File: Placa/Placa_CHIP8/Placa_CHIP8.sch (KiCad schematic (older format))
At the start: 10 parts, among them J1 Conn_01x08_Male-Teclado-Matri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, J2 Conn_01x06_Female-SD, J3 Conn_01x20_Female_LCD, J4 Conn_01x03_Male-UART, Q1 BC337, U1 STM32F103C8Tx, U2 Fuente

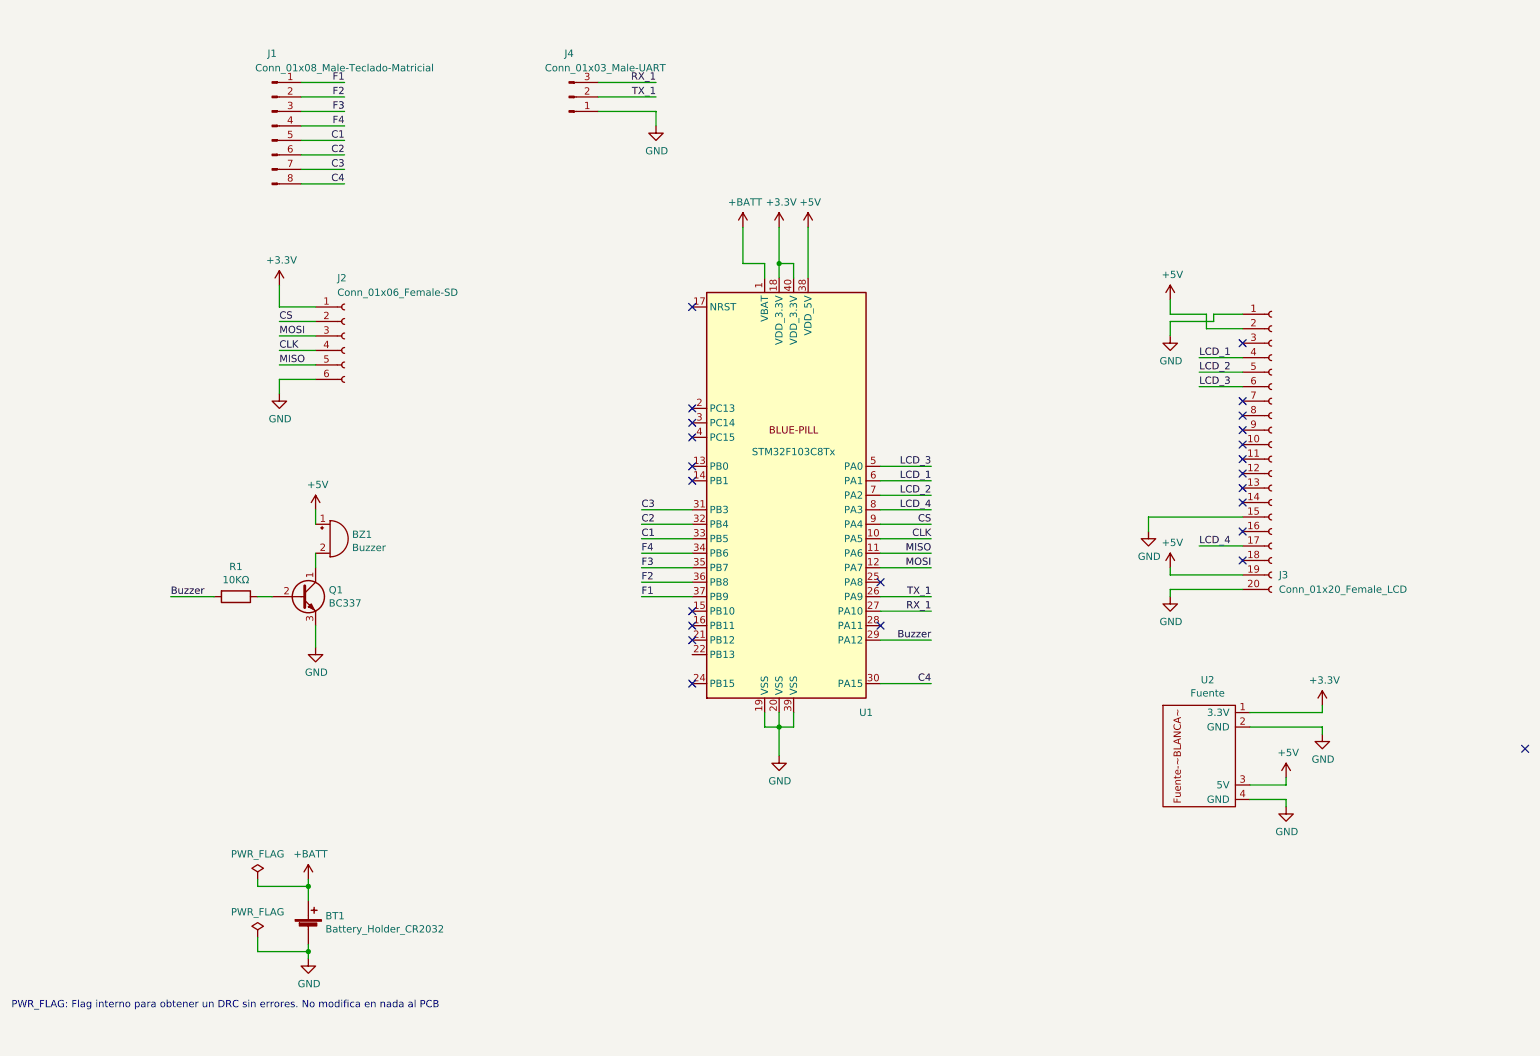
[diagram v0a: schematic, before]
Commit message: Modifico Placa con las conexiones nuevas
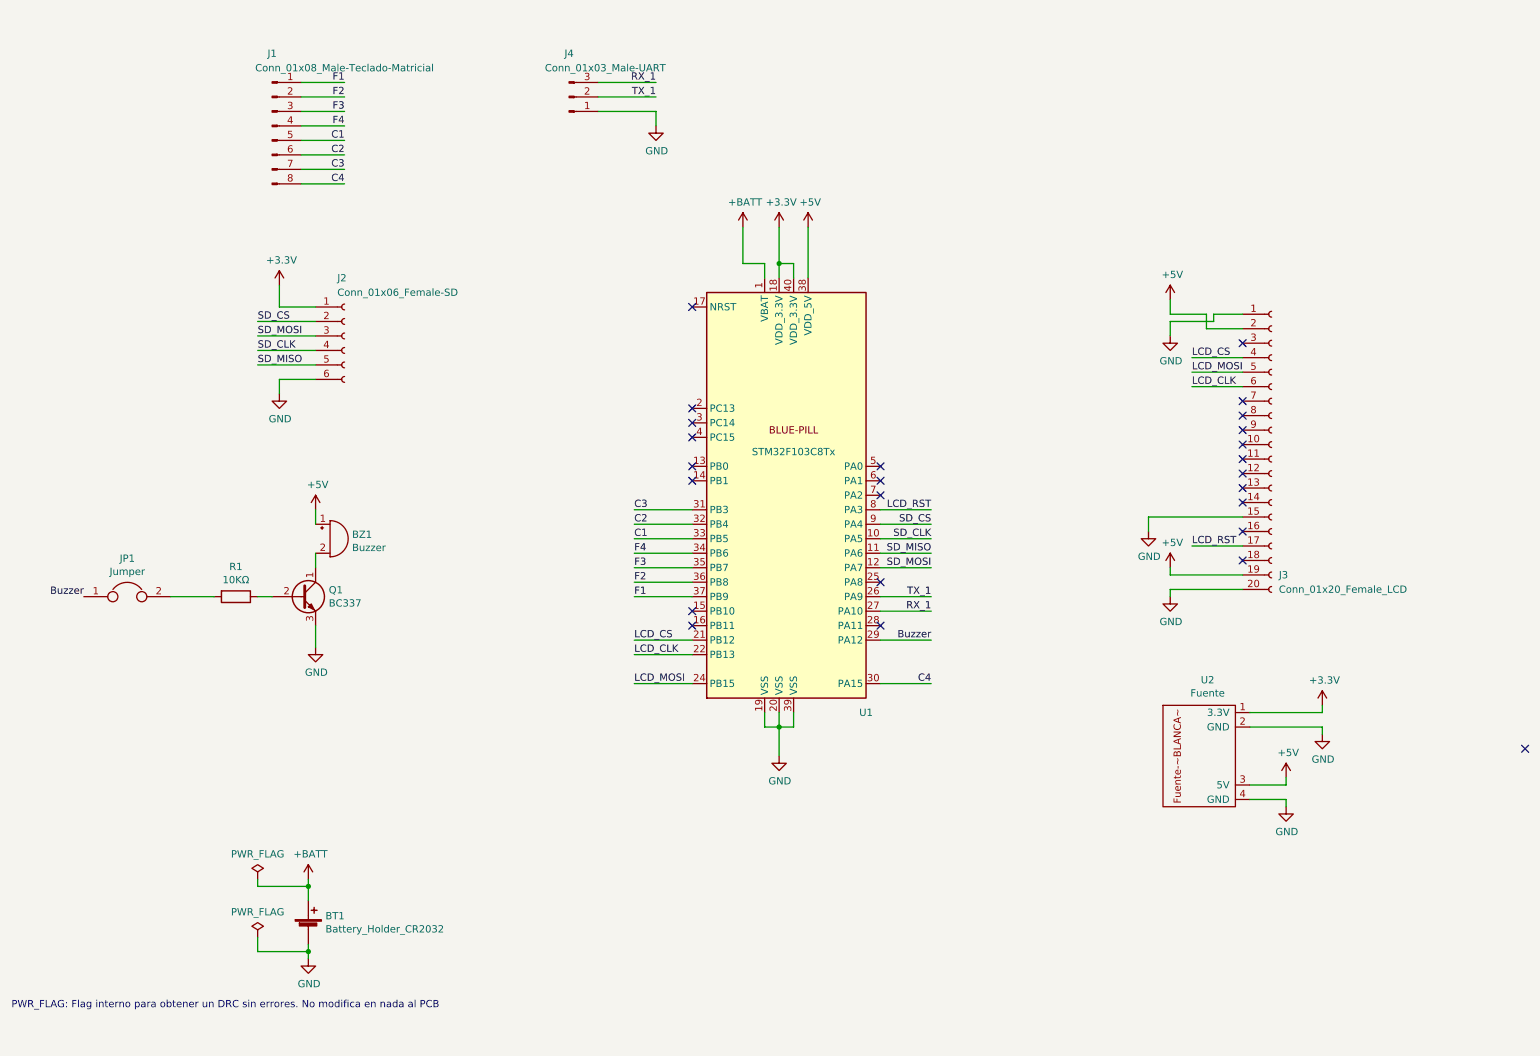
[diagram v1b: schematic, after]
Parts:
- added JP1: Jumper, symbol Device:Jumper
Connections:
- net Buzzer: now also JP1.1; no longer R1.2
- net LCD_CS: now reaches U1.21 (PB12)
- net LCD_CS: now also J3.4 (Pin_4)
- net LCD_CLK: now reaches U1.22 (PB13)
- net LCD_CLK: now also J3.6 (Pin_6)
- net LCD_MOSI: now reaches U1.24 (PB15)
- net LCD_MOSI: now also J3.5 (Pin_5)
- net CLK renamed SD_CLK
- net CS renamed SD_CS
- net LCD_1: no longer names the net of U1.6 (PA1)
- net LCD_1: no longer J3.4 (Pin_4)
- net LCD_2: no longer names the net of U1.7 (PA2)
- net LCD_2: no longer J3.5 (Pin_5)
- net LCD_3: no longer names the net of U1.5 (PA0)
- net LCD_3: no longer J3.6 (Pin_6)
- net LCD_4 renamed LCD_RST
- net MISO renamed SD_MISO
- net MOSI renamed SD_MOSI
- new net: JP1.2, R1.2
- no-connect marks 24 -> 25
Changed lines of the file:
@@
 Wire Wire Line
 	3100 1600 2800 1600
-Text Label 5150 3950 0    50   ~ 0
+Text Label 5100 3950 0    50   ~ 0
 C3
-Text Label 5150 4050 0    50   ~ 0
+Text Label 5100 4050 0    50   ~ 0
 C2
-Text Label 5150 4150 0    50   ~ 0
+Text Label 5100 4150 0    50   ~ 0
 C1
-Text Label 5150 4250 0    50   ~ 0
+Text Label 5100 4250 0    50   ~ 0
 F4
-Text Label 5150 4350 0    50   ~ 0
+Text Label 5100 4350 0    50   ~ 0
 F3
-Text Label 5150 4450 0    50   ~ 0
+Text Label 5100 4450 0    50   ~ 0
 F2
-Text Label 5150 4550 0    50   ~ 0
+Text Label 5100 4550 0    50   ~ 0
 F1
 Wire Wire Line
-	2900 2650 2650 2650
-Wire Wire Line
 	2900 2550 2650 2550
-Wire Wire Line
-	2900 2750 2650 2750
-Wire Wire Line
-	2900 2850 2650 2850
-Wire Wire Line
-	2900 2950 2650 2950
 Wire Wire Line
 	2900 3050 2650 3050
@@
 Wire Wire Line
 	2650 2400 2650 2550
-Text Label 2650 2950 0    50   ~ 0
-MISO
-Text Label 2650 2850 0    50   ~ 0
-CLK
-Text Label 2650 2750 0    50   ~ 0
-MOSI
-Text Label 2650 2650 0    50   ~ 0
-CS
+Text Label 2500 2950 0    50   ~ 0
+SD_MISO
+Text Label 2500 2850 0    50   ~ 0
+SD_CLK
+Text Label 2500 2750 0    50   ~ 0
+SD_MOSI
+Text Label 2500 2650 0    50   ~ 0
+SD_CS
 $Comp
 L Device:Buzzer BZ1
@@
 Wire Wire Line
 	2200 4550 1900 4550
-Text Label 1900 4550 0    50   ~ 0
+Text Label 1300 4550 2    50   ~ 0
 Buzzer
 $Comp
@@
 	2850 6950 2850 7000
 Wire Wire Line
-	9000 2900 9300 2900
-Wire Wire Line
-	9000 3000 9300 3000
-Wire Wire Line
-	9000 3100 9300 3100
-Wire Wire Line
 	9300 4400 8800 4400
 $Comp
@@
 Wire Wire Line
 	8800 4400 8800 4350
-Wire Wire Line
-	9300 4200 9000 4200
 $Comp
 L power:GND #PWR0110
@@
 NoConn ~ 9300 4100
 NoConn ~ 9300 4300
-Text Label 9000 2900 0    50   ~ 0
-LCD_1
-Text Label 9000 3000 0    50   ~ 0
-LCD_2
-Text Label 9000 3100 0    50   ~ 0
-LCD_3
-Text Label 9000 4200 0    50   ~ 0
-LCD_4
+Text Label 8950 2900 0    50   ~ 0
+LCD_CS
+Text Label 8950 4200 0    50   ~ 0
+LCD_RST
 Text Label 7150 4850 2    50   ~ 0
 Buzzer
-Text Label 7150 3850 2    50   ~ 0
-LCD_2
 Text Label 7150 3950 2    50   ~ 0
-LCD_4
-Text Label 7150 3750 2    50   ~ 0
-LCD_1
-Text Label 7150 3650 2    50   ~ 0
-LCD_3
+LCD_RST
 Text Label 7150 4050 2    50   ~ 0
-CS
+SD_CS
 Text Label 7150 4150 2    50   ~ 0
-CLK
-Text Label 7150 4250 2    50   ~ 0
-MISO
-Text Label 7150 4350 2    50   ~ 0
-MOSI
+SD_CLK
 $Comp
 L power:+5V #PWR0111
@@
 NoConn ~ 6800 4750
 NoConn ~ 5500 4650
-NoConn ~ 5500 4750
-NoConn ~ 5500 4850
-NoConn ~ 5500 5150
 NoConn ~ 5500 3750
 NoConn ~ 5500 3650
@@
 PWR_FLAG: Flag interno para obtener un DRC sin errores. No modifica en nada al PCB
 Wire Wire Line
-	6800 3650 7150 3650
-Wire Wire Line
-	6800 3750 7150 3750
-Wire Wire Line
-	6800 3850 7150 3850
-Wire Wire Line
 	6800 3950 7150 3950
 Wire Wire Line
@@
 Wire Wire Line
 	6800 5150 7150 5150
-Wire Wire Line
-	5150 4550 5500 4550
-Wire Wire Line
-	5150 4450 5500 4450
-Wire Wire Line
-	5150 4350 5500 4350
-Wire Wire Line
-	5150 4250 5500 4250
-Wire Wire Line
-	5150 4150 5500 4150
-Wire Wire Line
-	5150 4050 5500 4050
-Wire Wire Line
-	5150 3950 5500 3950
 Wire Wire Line
 	6800 4650 7150 4650
@@
 	1    0    0    -1
 $EndComp
+Wire Wire Line
+	2500 2650 2900 2650
+Wire Wire Line
+	2500 2750 2900 2750
+Wire Wire Line
+	2500 2850 2900 2850
+Wire Wire Line
+	2500 2950 2900 2950
+Text Label 7150 4250 2    50   ~ 0
+SD_MISO
+Text Label 7150 4350 2    50   ~ 0
+SD_MOSI
+NoConn ~ 5500 4750
+Text Label 5100 4850 0    50   ~ 0
+LCD_CS
+Text Label 5100 5150 0    50   ~ 0
+LCD_MOSI
+Wire Wire Line
+	5100 3950 5500 3950
+Wire Wire Line
+	5100 4050 5500 4050
+Wire Wire Line
+	5100 4150 5500 4150
+Wire Wire Line
+	5100 4250 5500 4250
+Wire Wire Line
+	5100 4350 5500 4350
+Wire Wire Line
+	5100 4450 5500 4450
+Wire Wire Line
+	5100 4550 5500 4550
+Wire Wire Line
+	5100 4850 5500 4850
+Wire Wire Line
+	5100 5150 5500 5150
+Wire Wire Line
+	5500 4950 5100 4950
+Text Label 5100 4950 0    50   ~ 0
+LCD_CLK
+NoConn ~ 6800 3650
+NoConn ~ 6800 3750
+NoConn ~ 6800 3850
+Wire Wire Line
+	8950 4200 9300 4200
+Wire Wire Line
+	8950 3100 9300 3100
+Wire Wire Line
+	9300 3000 8950 3000
+Wire Wire Line
+	8950 2900 9300 2900
+Text Label 8950 3000 0    50   ~ 0
+LCD_MOSI
+Text Label 8950 3100 0    50   ~ 0
+LCD_CLK
+$Comp
+L Device:Jumper JP1
+U 1 1 617816B8
+P 1600 4550
+F 0 "JP1" H 1600 4814 50  0000 C CNN
+F 1 "Jumper" H 1600 4723 50  0000 C CNN
+F 2 "" H 1600 4550 50  0001 C CNN
+F 3 "~" H 1600 4550 50  0001 C CNN
+	1    1600 4550
+	1    0    0    -1
+$EndComp

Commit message: modif
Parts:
- JP1: footprint (none) -> Connector_PinHeader_2.54mm:PinHeader_1x02_P2.54mm_Vertical
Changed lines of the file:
@@
 F 0 "JP1" H 1600 4814 50  0000 C CNN
 F 1 "Jumper" H 1600 4723 50  0000 C CNN
-F 2 "" H 1600 4550 50  0001 C CNN
+F 2 "Connector_PinHeader_2.54mm:PinHeader_1x02_P2.54mm_Vertical" H 1600 4550 50  0001 C CNN
 F 3 "~" H 1600 4550 50  0001 C CNN
 	1    1600 4550

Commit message: Agrego modelo Willy funcando ok y V1 gabinete
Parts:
- BT1: symbol Device:Battery_Cell -> Placa_CHIP8-rescue:Battery_Cell-Device
- BZ1: symbol Device:Buzzer -> Placa_CHIP8-rescue:Buzzer-Device
- J1: symbol Connector:Conn_01x08_Male -> Placa_CHIP8-rescue:Conn_01x08_Male-Connector
- J2: symbol Connector:Conn_01x06_Female -> Placa_CHIP8-rescue:Conn_01x06_Female-Connector
- J3: symbol Connector:Conn_01x20_Female -> Placa_CHIP8-rescue:Conn_01x20_Female-Connector
- J4: symbol Connector:Conn_01x03_Male -> Placa_CHIP8-rescue:Conn_01x03_Male-Connector
- JP1: symbol Device:Jumper -> Placa_CHIP8-rescue:Jumper-Device
- Q1: symbol Transistor_BJT:BC337 -> Placa_CHIP8-rescue:BC337-Transistor_BJT
- R1: symbol Device:R -> Placa_CHIP8-rescue:R-Device
- U1: symbol Placa:STM32F103C8Tx -> Placa_CHIP8-rescue:STM32F103C8Tx-Placa
- U2: symbol Placa:Fuente -> Placa_CHIP8-rescue:Fuente-Placa
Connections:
- wire segments 92 -> 98
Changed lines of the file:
@@
 $EndDescr
 $Comp
-L Connector:Conn_01x08_Male J1
+L Placa_CHIP8-rescue:Conn_01x08_Male-Connector J1
 U 1 1 61500CE4
 P 2600 1300
@@
 	2650 3050 2650 3150
 $Comp
-L power:GND #PWR0101
+L Placa_CHIP8-rescue:GND-power #PWR0101
 U 1 1 61511F8F
 P 2650 3150
@@
 $EndComp
 $Comp
-L power:+3.3V #PWR0102
+L Placa_CHIP8-rescue:+3.3V-power #PWR0102
 U 1 1 615124CF
 P 2650 2400
@@
 SD_CS
 $Comp
-L Device:Buzzer BZ1
+L Placa_CHIP8-rescue:Buzzer-Device BZ1
 U 1 1 61517873
 P 3000 4150
@@
 $EndComp
 $Comp
-L Transistor_BJT:BC337 Q1
+L Placa_CHIP8-rescue:BC337-Transistor_BJT Q1
 U 1 1 61518038
 P 2800 4550
@@
 $EndComp
 $Comp
-L power:GND #PWR0103
+L Placa_CHIP8-rescue:GND-power #PWR0103
 U 1 1 615193E1
 P 2900 4900
@@
 $EndComp
 $Comp
-L Device:R R1
+L Placa_CHIP8-rescue:R-Device R1
 U 1 1 61519A86
 P 2350 4550
@@
 $EndComp
 $Comp
-L power:+5V #PWR0104
+L Placa_CHIP8-rescue:+5V-power #PWR0104
 U 1 1 6151A6DF
 P 2900 3950
@@
 Wire Wire Line
 	2600 4550 2500 4550
-Wire Wire Line
-	2200 4550 1900 4550
 Text Label 1300 4550 2    50   ~ 0
 Buzzer
 $Comp
-L Device:Battery_Cell BT1
+L Placa_CHIP8-rescue:Battery_Cell-Device BT1
 U 1 1 615277F3
 P 2850 6850
@@
 $EndComp
 $Comp
-L power:GND #PWR0105
+L Placa_CHIP8-rescue:GND-power #PWR0105
 U 1 1 6152B7C4
 P 2850 7050
@@
 	9300 4400 8800 4400
 $Comp
-L power:+5V #PWR0108
+L Placa_CHIP8-rescue:+5V-power #PWR0108
 U 1 1 61553D8C
 P 8800 4350
@@
 $EndComp
 $Comp
-L power:GND #PWR0109
+L Placa_CHIP8-rescue:GND-power #PWR0109
 U 1 1 61554437
 P 8800 4550
@@
 	8800 4400 8800 4350
 $Comp
-L power:GND #PWR0110
+L Placa_CHIP8-rescue:GND-power #PWR0110
 U 1 1 6155A581
 P 8650 4100
@@
 SD_CLK
 $Comp
-L power:+5V #PWR0111
+L Placa_CHIP8-rescue:+5V-power #PWR0111
 U 1 1 61591E63
 P 9600 5800
@@
 $EndComp
 $Comp
-L power:GND #PWR0112
+L Placa_CHIP8-rescue:GND-power #PWR0112
 U 1 1 6159276C
 P 9600 6000
@@
 $EndComp
 $Comp
-L power:+3.3V #PWR0113
+L Placa_CHIP8-rescue:+3.3V-power #PWR0113
 U 1 1 6159301E
 P 9850 5300
@@
 $EndComp
 $Comp
-L power:GND #PWR0114
+L Placa_CHIP8-rescue:GND-power #PWR0114
 U 1 1 61593D3E
 P 9850 5500
@@
 	9600 5950 9600 6000
 $Comp
-L power:GND #PWR0115
+L Placa_CHIP8-rescue:GND-power #PWR0115
 U 1 1 615AC362
 P 6100 5650
@@
 	6100 5650 6100 5450
 $Comp
-L power:+3.3V #PWR0116
+L Placa_CHIP8-rescue:+3.3V-power #PWR0116
 U 1 1 615B6A0C
 P 6100 2000
@@
 NoConn ~ 11250 5600
 $Comp
-L power:+BATT #PWR0117
+L Placa_CHIP8-rescue:+BATT-power #PWR0117
 U 1 1 615E3802
 P 2850 6500
@@
 	2850 6500 2850 6550
 $Comp
-L power:+BATT #PWR0118
+L Placa_CHIP8-rescue:+BATT-power #PWR0118
 U 1 1 615E9338
 P 5850 2000
@@
 $EndComp
 $Comp
-L Placa:Fuente U2
+L Placa_CHIP8-rescue:Fuente-Placa U2
 U 1 1 615EFB9F
 P 9000 5650
@@
 $EndComp
 $Comp
-L Placa:STM32F103C8Tx U1
+L Placa_CHIP8-rescue:STM32F103C8Tx-Placa U1
 U 1 1 6160BC1E
 P 6200 3850
@@
 $EndComp
 $Comp
-L power:+5V #PWR0119
+L Placa_CHIP8-rescue:+5V-power #PWR0119
 U 1 1 61620457
 P 6300 2000
@@
 	2850 6550 2850 6650
 $Comp
-L power:PWR_FLAG #FLG0102
+L Placa_CHIP8-rescue:PWR_FLAG-power #FLG0102
 U 1 1 6162B3A1
 P 2500 6900
@@
 TX_1
 $Comp
-L Connector:Conn_01x03_Male J4
+L Placa_CHIP8-rescue:Conn_01x03_Male-Connector J4
 U 1 1 615256F9
 P 4650 1100
@@
 	5250 1200 5250 1300
 $Comp
-L power:GND #PWR0120
+L Placa_CHIP8-rescue:GND-power #PWR0120
 U 1 1 61533673
 P 5250 1300
@@
 	1    0    0    -1
 $EndComp
-Text Label 5250 1100 2    50   ~ 0
+Text Label 5550 1100 2    50   ~ 0
 TX_1
 Wire Wire Line
-	4850 1100 5250 1100
-Wire Wire Line
-	4850 1000 5250 1000
-Wire Wire Line
 	4850 1200 5250 1200
 $Comp
-L Connector:Conn_01x20_Female J3
+L Placa_CHIP8-rescue:Conn_01x20_Female-Connector J3
 U 1 1 6152DDD6
 P 9500 3500
@@
 $EndComp
 $Comp
-L power:GND #PWR0106
+L Placa_CHIP8-rescue:GND-power #PWR0106
 U 1 1 615368BB
 P 8800 2750
@@
 $EndComp
 $Comp
-L power:+5V #PWR0107
+L Placa_CHIP8-rescue:+5V-power #PWR0107
 U 1 1 6153D9CC
 P 8800 2500
@@
 	8800 2500 8800 2600
 $Comp
-L Connector:Conn_01x06_Female J2
+L Placa_CHIP8-rescue:Conn_01x06_Female-Connector J2
 U 1 1 6150C5A6
 P 3100 2750
@@
 	1    0    0    -1
 $EndComp
-Text Label 5250 1000 2    50   ~ 0
+Text Label 5550 1000 2    50   ~ 0
 RX_1
 Wire Wire Line
@@
 	2500 6500 2500 6550
 $Comp
-L power:PWR_FLAG #FLG0101
+L Placa_CHIP8-rescue:PWR_FLAG-power #FLG0101
 U 1 1 61628B00
 P 2500 6500
@@
 LCD_CLK
 $Comp
-L Device:Jumper JP1
+L Placa_CHIP8-rescue:Jumper-Device JP1
 U 1 1 617816B8
 P 1600 4550
@@
 	1    0    0    -1
 $EndComp
+Wire Wire Line
+	4850 1000 5200 1000
+Wire Wire Line
+	5200 1000 5200 1100
+Wire Wire Line
+	5200 1100 5550 1100
+Wire Wire Line
+	2200 4550 1900 4550
+Wire Wire Line
+	4850 1100 5100 1100
+Wire Wire Line
+	5100 1100 5100 1050
+Wire Wire Line
+	5100 1050 5300 1050
+Wire Wire Line
+	5300 1050 5300 1000
+Wire Wire Line
+	5300 1000 5550 1000
 $EndSCHEMATC
